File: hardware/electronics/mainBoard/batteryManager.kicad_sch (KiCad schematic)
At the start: 39 parts, among them J10 S3B-XH-SM4-TB, J9 1726480102, Q2 BUK6D72-30EX, Q3 NXV90EP, Q4 BUK6D72-30EX, Q5 2N7002NXAK, U13 BQ40Z50-R2

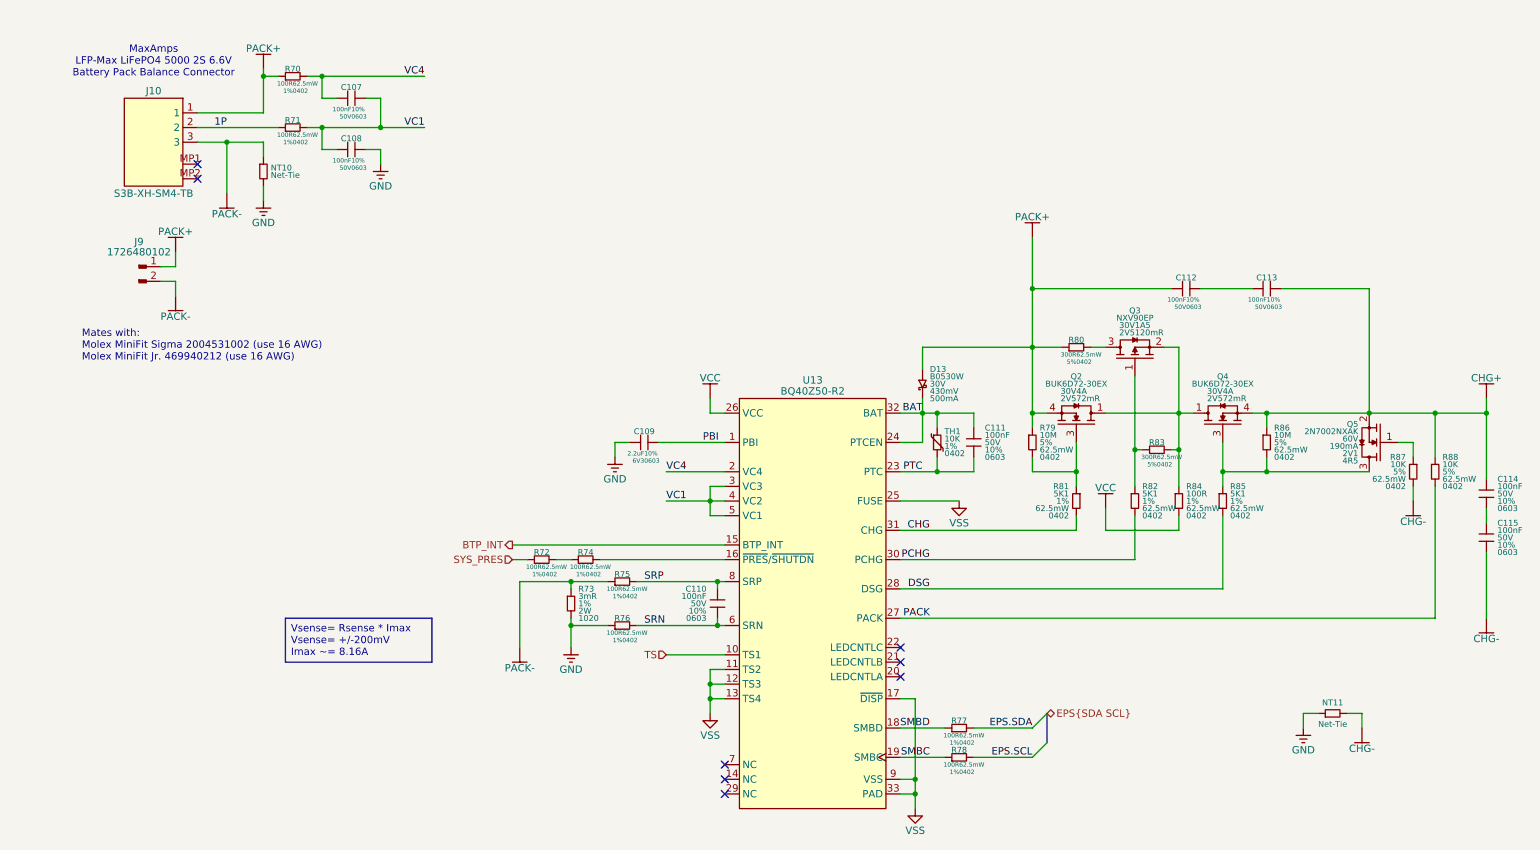
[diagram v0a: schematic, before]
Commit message: replaced balancer IC
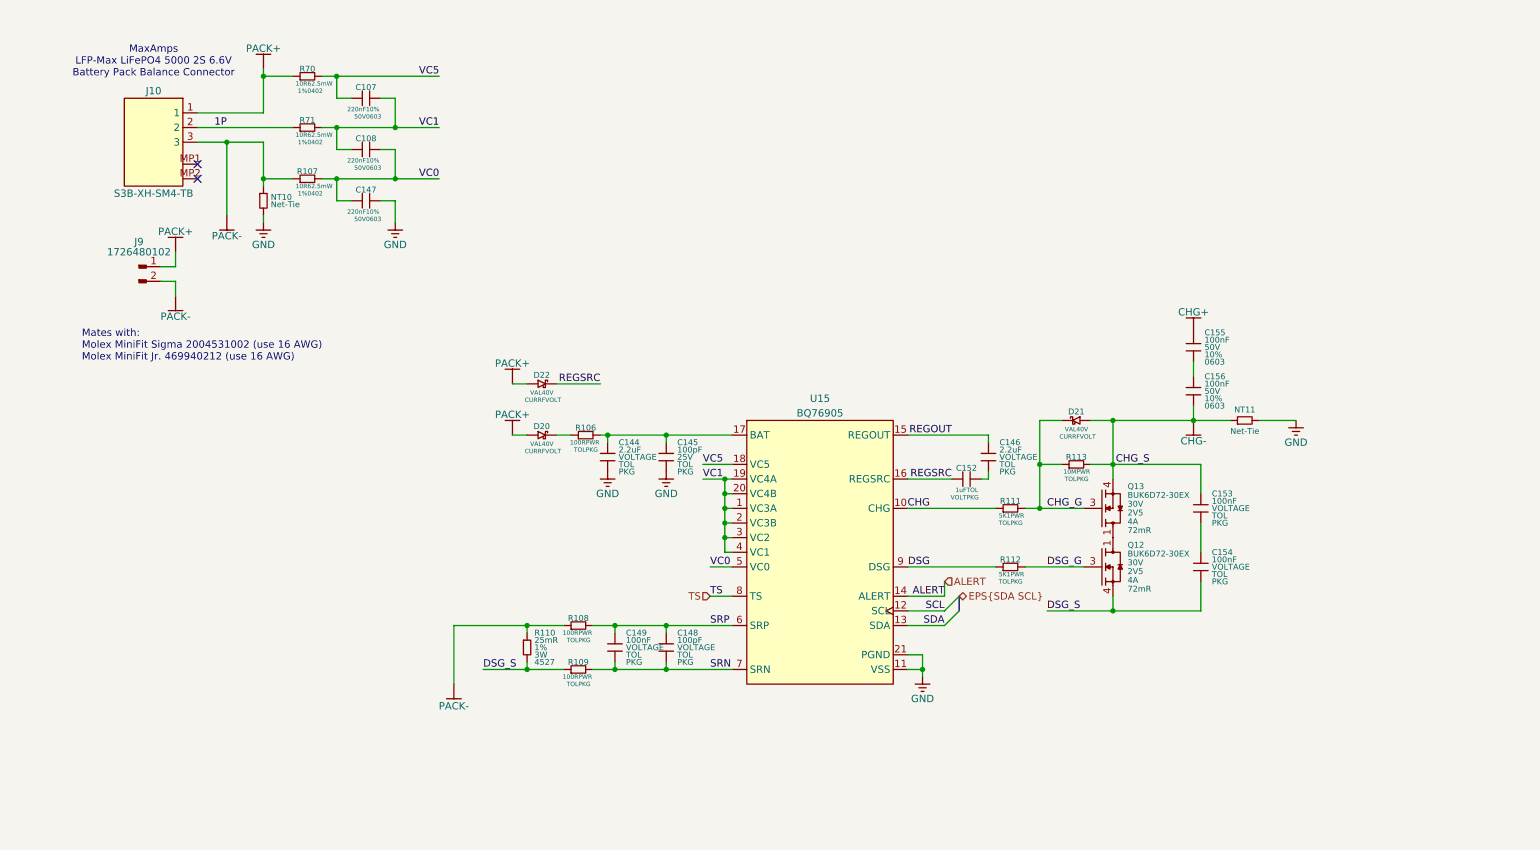
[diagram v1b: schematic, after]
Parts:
- removed C109: 2.2uF, lib_fp:MLCC0603, symbol lib_sch:C_horizontal
- removed C110, C111, C114, C115: 100nF, lib_fp:MLCC0603, symbol lib_sch:C
- removed C112, C113: 100nF, lib_fp:MLCC0603, symbol lib_sch:C_horizontal
- removed D13: B0530W, lib_fp:SOD123, symbol lib_sch:D_Schottky
- removed Q2, Q4: BUK6D72-30EX, lib_fp:UDFN6P65_200X200X65L30X25N, symbol lib_sch:NMOS_DGS
- removed Q3: NXV90EP, lib_fp:SOT23-3P95_230X290X100L43X30N, symbol lib_sch:PMOS_GSD
- removed Q5: 2N7002NXAK, lib_fp:SOT23-3P95_230X290X100L43X30N, symbol lib_sch:NMOS_GSD
- removed R72, R74, R75, R76, R77, R78: 100R, lib_fp:CRCW0402, symbol lib_sch:R_horizontal
- removed R73: 3mR, lib_fp:WSL1020, symbol lib_sch:R
- removed R79, R86: 10M, lib_fp:CRCW0402, symbol lib_sch:R
- removed R80, R83: 300R, lib_fp:CRCW0402, symbol lib_sch:R_horizontal
- removed R81, R82, R85: 5K1, lib_fp:CRCW0402, symbol lib_sch:R
- removed R84: 100R, lib_fp:CRCW0402, symbol lib_sch:R
- removed R87, R88: 10K, lib_fp:CRCW0402, symbol lib_sch:R
- removed TH1: 10K, lib_fp:SON2P65_100X60X50L50X25N, symbol lib_sch:Thermistor
- removed U13: BQ40Z50-R2, lib_fp:RSM0032A, symbol lib_sch:BQ40Z50-R2
- added C144, C146: 2.2uF, symbol lib_sch:C
- added C145, C148: 100pF, symbol lib_sch:C
- added C147: 220nF, lib_fp:MLCC0603, symbol lib_sch:C_horizontal
- added C149, C153, C154: 100nF, symbol lib_sch:C
- added C152: 1uF, symbol lib_sch:C_horizontal
- added C155, C156: 100nF, lib_fp:MLCC0603, symbol lib_sch:C
- added D20, D21, D22: VAL, symbol .DS-Diodes:D_Schottky_horizontal
- added Q12, Q13: BUK6D72-30EX, lib_fp:UDFN6P65_200X200X65L30X25N, symbol lib_sch:NMOS_DGS
- added R106, R108, R109: 100R, symbol lib_sch:R_horizontal
- added R107: 10R, lib_fp:CRCW0402, symbol lib_sch:R_horizontal
- added R110: 25mR, symbol lib_sch:R
- added R111, R112: 5K1, symbol lib_sch:R_horizontal
- added R113: 10M, symbol lib_sch:R_horizontal
- added U15: BQ76905, symbol .DS-PMIC:BQ76905
- C107, C108: value 100nF -> 220nF
- R70, R71: value 100R -> 10R
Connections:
- net CHG: now also R111.1, U15.10 (CHG)
- net CHG+: now also C155.1
- net CHG-: now also NT11.1, C153.1, C156.2, D21.1, Q13.4, Q13.8, R113.2; no longer NT11.2
- net DSG: now also R112.1, U15.9 (DSG)
- net GND: now also NT11.2, C144.2, C145.2, C147.2, U15.11 (VSS), U15.21 (PGND); no longer C108.2, NT11.1
- net PACK+: now also D20.1, D22.1
- net PACK-: now also R107.1, R108.1, R110.1
- net SRN: now also C148.2, C149.2, R109.2, U15.7 (SRN)
- net SRP: now also C148.1, C149.1, R108.2, U15.6 (SRP)
- net TS: now also U15.8 (TS)
- net VC1: now also U15.1 (VC3A), U15.19 (VC4A), U15.2 (VC3B), U15.20 (VC4B), U15.3 (VC2), U15.4 (VC1)
- net VC4 renamed VC5
- net VC5: now also U15.18 (VC5)
- new net: C155.2, C156.1
- new net: C153.2, C154.1
- new net: D20.2, R106.1
- new net: C144.1, C145.1, R106.2, U15.17 (BAT)
- new net: C146.2, C152.2
- new net: Q12.1, Q12.2, Q12.5, Q12.6, Q12.7, Q13.1, Q13.2, Q13.5, Q13.6, Q13.7
- new net ALERT: U15.14 (ALERT)
- new net CHG_G: D21.2, Q13.3, R111.2, R113.1
- new net DSG_G: Q12.3, R112.2
- new net DSG_S: C154.2, Q12.4, Q12.8, R109.1, R110.2
- new net REGOUT: C146.1, U15.15 (REGOUT)
- new net REGSRC: C152.1, D22.2, U15.16 (REGSRC)
- new net SCL: U15.12 (SCL)
- new net SDA: U15.13 (SDA)
- new net VC0: C108.2, C147.1, R107.2, U15.5 (VC0)
- no-connect marks 8 -> 2
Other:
- title: (none) -> Battery Monitor and Protector
- moved on the sheet: C107, C108, NT10, NT11, R70, R71

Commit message: replaced manager. sheet pins
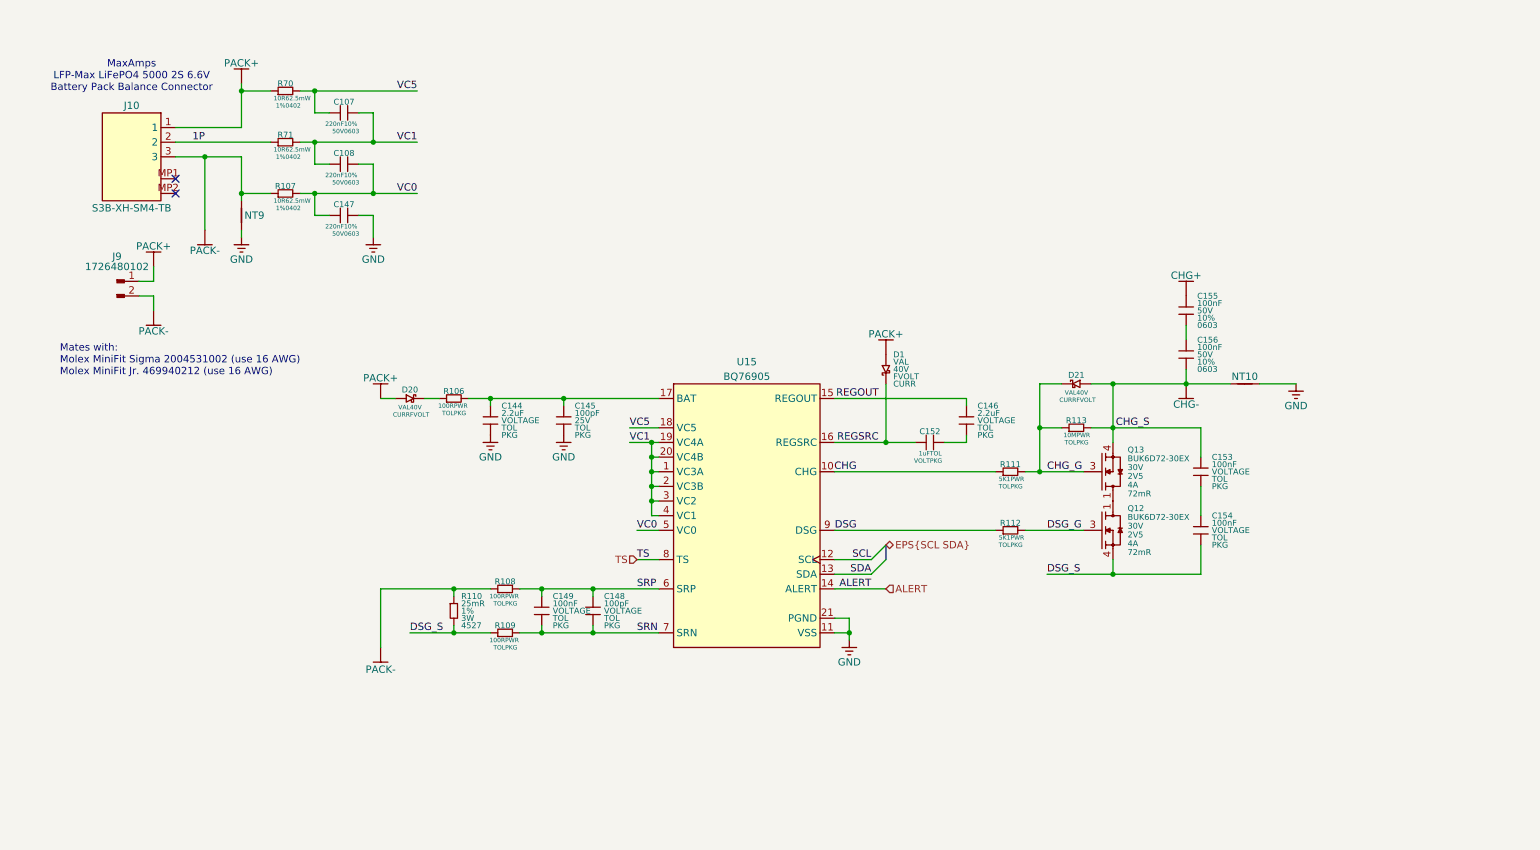
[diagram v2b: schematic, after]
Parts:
- removed D22: VAL, symbol .DS-Diodes:D_Schottky_horizontal
- removed NT10, NT11: Net-Tie, lib_fp:NetTie-2_SMD_Pad2.0mm, symbol lib_sch:NT
- added D1: VAL, symbol lib_sch:D_Schottky
- added NT10, NT9: NetTie_2, symbol lib_sch:NetTie_2
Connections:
- net CHG-: now also NT10.1
- net GND: now also NT10.2, NT9.2
- net PACK+: now also D1.1
- net PACK-: now also NT9.1
- net REGSRC: now also D1.2
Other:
- moved on the sheet: C107, C108, C144, C145, C146, C147, C148, C149, C152, C153, C154, C155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

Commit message: added new battery manager
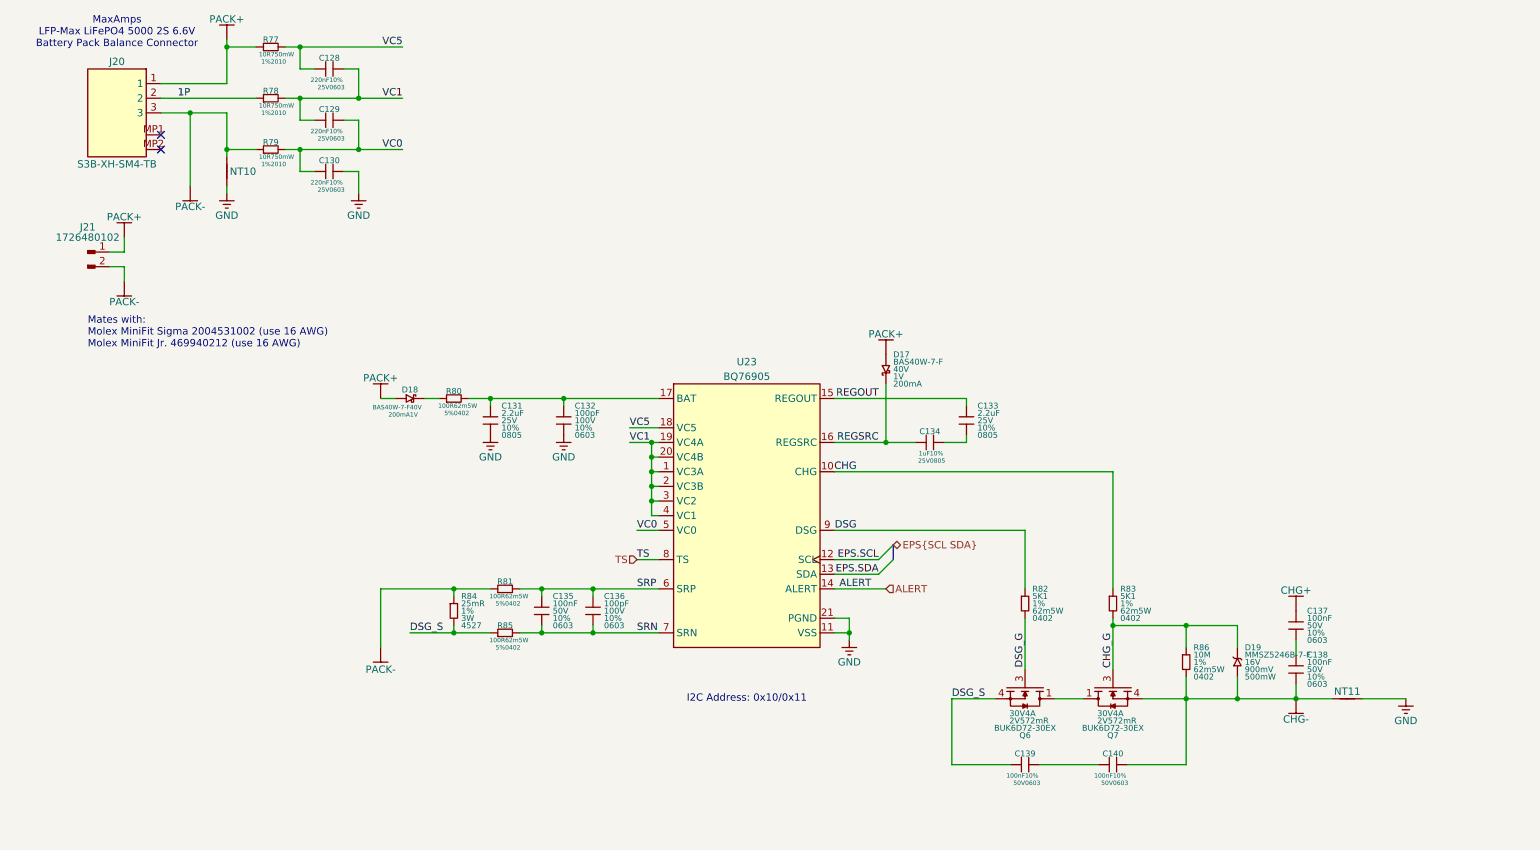
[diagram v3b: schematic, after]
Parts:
- removed C145: 100pF, symbol lib_sch:C
- removed C146: 2.2uF, symbol lib_sch:C
- removed C149, C153, C154: 100nF, symbol lib_sch:C
- removed D21: VAL, symbol .DS-Diodes:D_Schottky_horizontal
- removed Q12, Q13: BUK6D72-30EX, lib_fp:UDFN6P65_200X200X65L30X25N, symbol lib_sch:NMOS_DGS
- removed R106, R108, R109: 100R, symbol lib_sch:R_horizontal
- removed R107, R71: 10R, lib_fp:CRCW0402, symbol lib_sch:R_horizontal
- removed R111, R112: 5K1, symbol lib_sch:R_horizontal
- removed R113: 10M, symbol lib_sch:R_horizontal
- added C132: 100pF, symbol lib_sch:C
- added C133: 2.2uF, symbol lib_sch:C
- added C135: 100nF, symbol lib_sch:C
- added C139, C140: 100nF, symbol lib_sch:C_horizontal
- added D19: MMSZ5246B-7-F, symbol lib_sch:D_Zener
- added Q6, Q7: BUK6D72-30EX, symbol lib_sch:NMOS_DGS
- added R78, R79: 10R, symbol lib_sch:R_horizontal
- added R80, R81, R85: 100R, symbol lib_sch:R_horizontal
- added R82, R83: 5K1, symbol lib_sch:R
- added R86: 10M, symbol lib_sch:R
- C128: renamed from C107; footprint lib_fp:MLCC0603 -> (none); DKPN 478-KAM15AR71H104KMCT-ND -> 478-KAM15BR71E224KTCT-ND; MPN KAM15AR71H104KM -> KAM15BR71E224KT; Tolerace 10% -> (none); Tolerance (none) -> 10%; Voltage Rating 50V -> 25V
- C129: renamed from C108; footprint lib_fp:MLCC0603 -> (none); DKPN 478-KAM15AR71H104KMCT-ND -> 478-KAM15BR71E224KTCT-ND; MPN KAM15AR71H104KM -> KAM15BR71E224KT; Tolerace 10% -> (none); Tolerance (none) -> 10%; Voltage Rating 50V -> 25V
- C130: renamed from C147; footprint lib_fp:MLCC0603 -> (none); DKPN 478-KAM15AR71H104KMCT-ND -> 478-KAM15BR71E224KTCT-ND; MPN KAM15AR71H104KM -> KAM15BR71E224KT; Tolerace 10% -> (none); Tolerance (none) -> 10%; Voltage Rating 50V -> 25V
- C131: renamed from C144; DKPN (none) -> 478-KAM21KR71E225KUCT-ND; MPN (none) -> 08053C225K4T2A; Manufacturer (none) -> KYOCERA AVX; Package PKG -> 0805; Tolerance TOL -> 10%; Voltage Rating VOLTAGE -> 25V
- C134: renamed from C152; DKPN (none) -> 478-KAF21KR71E105KLCT-ND; MPN (none) -> 08053C105K4Z4A; Manufacturer (none) -> KYOCERA AVX; Package PKG -> 0805; Tolerace TOL -> (none); Tolerance (none) -> 10%; Voltage Rating VOLT -> 25V
- C136: renamed from C148; DKPN (none) -> 478-06031C101K4T2ACT-ND; MPN (none) -> 06031C101K4T2A; Manufacturer (none) -> KYOCERA AVX; Package PKG -> 0603; Tolerance TOL -> 10%; Voltage Rating VOLTAGE -> 100V
- C137: renamed from C155; footprint lib_fp:MLCC0603 -> (none); MPN KAM15AR71H104KM -> 06035C104K4T2A
- C138: renamed from C156; footprint lib_fp:MLCC0603 -> (none); MPN KAM15AR71H104KM -> 06035C104K4T2A
- D17: renamed from D1; value VAL -> BAS40W-7-F; Current CURR -> 200mA; DKPN (none) -> BAS40W-FDICT-ND; Forward Voltage FVOLT -> 1V; MPN (none) -> BAS40W-7-F; Manufacturer (none) -> Diodes Incorporated
- D18: renamed from D20; value VAL -> BAS40W-7-F; symbol .DS-Diodes:D_Schottky_horizontal -> lib_sch:D_Schottky_horizontal; Current CURR -> 200mA; DKPN (none) -> BAS40W-FDICT-ND; Forward Voltage FVOLT -> 1V; MPN (none) -> BAS40W-7-F; Manufacturer (none) -> Diodes Incorporated
- J20: renamed from J10; footprint lib_fp:JST_XH_S3B-SM4-TB -> (none)
- J21: renamed from J9; footprint lib_fp:1726480102 -> (none)
- R77: renamed from R70; footprint lib_fp:CRCW0402 -> (none); DKPN 541-100LCT-ND -> 541-10.0ACCT-ND; MPN CRCW0402100RFKED -> CRCW201010R0FKEF; Package 0402 -> 2010; Power Rating 62.5mW -> 750mW
- U23: renamed from U15; symbol .DS-PMIC:BQ76905 -> lib_sch:BQ76905; DKPN (none) -> 296-BQ76905RGRRCT-ND; MPN (none) -> BQ76905RGRR; Manufacturer (none) -> Texas Instruments
- renumbered NT9 to NT10, NT10 to NT11, R110 to R84
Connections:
- net 1P: now also R78.1
- net CHG: now also R83.1
- net CHG-: now also C140.2, D19.1, Q7.4, Q7.8, R86.2
- net CHG_G: now also D19.2, Q7.3, R83.2, R86.1
- net DSG: now also R82.1
- net DSG_G: now also Q6.3, R82.2
- net DSG_S: now also C139.1, Q6.4, Q6.8, R85.1
- net GND: now also C132.2
- net PACK-: now also R79.1, R81.1
- net REGOUT: now also C133.1
- net SRN: now also C135.2, R85.2
- net SRP: now also C135.1, R81.2
- net VC0: now also R79.2
- net VC1: now also R78.2
- net at D18.2: now also R80.1
- net at C131.1, U23.17 (BAT): now also C132.1, R80.2
- net at C134.2: now also C133.2
- net SCL renamed EPS.SCL
- net SDA renamed EPS.SDA
- new net: Q6.1, Q6.2, Q6.5, Q6.6, Q6.7, Q7.1, Q7.2, Q7.5, Q7.6, Q7.7
- new net: C139.2, C140.1
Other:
- note added: "I2C Address: 0x10/0x11"
- moved on the sheet: C128, C129, C130, C137, C138, J20, J21, NT10, NT11, R77

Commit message: cleaned
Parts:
- removed NT10, NT11: NetTie_2, symbol lib_sch:NetTie_2
- added NT11, NT12: NetTie, symbol lib_sch:NetTie
- C114: renamed from C137; DKPN 478-KAM15AR71H104KMCT-ND -> 478-KAM15AR71H104KTCT-ND
- C115: renamed from C138; DKPN 478-KAM15AR71H104KMCT-ND -> 478-KAM15AR71H104KTCT-ND
- renumbered C128 to C105, C129 to C106, C130 to C107, C131 to C108, C132 to C109, C133 to C110, C134 to C111, C135 to C112, C136 to C113, C139 to C116, C140 to C117, D17 to D16, D18 to D17, D19 to D18, Q6 to Q3, Q7 to Q4, R77 to R70, R78 to R71, R79 to R72, R80 to R73, R81 to R74, R82 to R75, R83 to R76, R84 to R77, R85 to R78, R86 to R79
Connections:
- net CHG-: now also NT11.1
- net GND: now also NT11.2, NT12.1
- net PACK-: now also NT12.2
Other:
- moved on the sheet: C114, C115
